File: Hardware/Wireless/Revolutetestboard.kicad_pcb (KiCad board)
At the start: 4 copper layers, 54 x 85.6 mm, 263 parts, among them J1 Conn_01x02_Pin, J2 Conn_01x02_Pin, J3 Conn_01x02_Pin, J4 Conn_01x04_Socket, J5 Conn_01x02_Pin, J6 Conn_01x04_Pin, J7 USB_C_Receptacle_USB2.0, J8 USB_C_Receptacle_USB2.0, J9 Conn_01x04_Socket, Q1 NMOS-CSD17381F4, Q10 PMOS-BSS84, Q2 NMOS-CSD17381F4, Q3 PMOS-CSD25483F4, Q4 PMOS-CSD25483F4, Q5 PMOS-CSD25483F4, Q7 PMOS-BSS84, Q8 IRLML6344, Q9 PMOS-BSS84, SW1 SW_DIP_x06, SW2 SW_DPDT_x2, SW3 SW_DIP_x06, SW4 SW_Push, SW5 SW_DPDT_x2, SW6 SW_DPDT_x2, U1 BQ27427, U10 battery_charger, U11 nRF52840_aQFN73, U12 TS5A3159AYZPR, U13 BQ27427, U14 TPS22910A, U15 A3144e, U16 A3144e, U18 pogopins, U19 LSM6DS3, U2 nrf52833_qfn40, U20 TPS54202DDC, U21 TPS54202DDC, U22 STM32F103CBTx, U23 AP2112K-3.3, U24 Conn_01x14_Socket, U25 TLV493D, U3 Conn_01x14_Socket, U4 TPS709, U5 AS5600, U6 BQ25180, U7 LSM6DSO, U8 TS5A3159AYZPR, U9 TPS22910A, X1 32.768 kHz, X2 32MHZ, X3 32.768 kHz, X4 32MHZ, Y1 32.768KHZ, Y2 8Mhz

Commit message: test board done
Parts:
- removed D3: RED_LED, LED_SMD:LED_0402_1005Metric
- removed R29: 1K, Resistor_SMD:R_0402_1005Metric
- added R58: 220r, Resistor_SMD:R_0402_1005Metric, F.Cu at (131.1, 130.5)
- added R59: 220r, Resistor_SMD:R_0402_1005Metric, F.Cu at (130.1, 130.7)
- added R7: 220r, Resistor_SMD:R_0402_1005Metric, F.Cu at (132.7, 130.2)
- added U26: 1615 RGB SMD LED, Library:1615 RGB SMD LED, F.Cu at (131.3, 128.2)
- moved JP7 0.23 mm to (132.4, 133.2)
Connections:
- U11 pad B13: /pod/P0.03 -> B-
- U11 pad B15: Net-(D3-A) -> G-
- U11 pad B19: unconnected-(U11-P1.11-PadB19) -> R-
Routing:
- net R-: track 0.00 -> 8.92 mm, vias 0 -> 2
- net Net-(D3-A): track 7.42 -> 0.00 mm, vias 2 -> 0
- net G-: track 0.00 -> 6.68 mm, vias 0 -> 2
- net B-: track 0.00 -> 5.74 mm, vias 0 -> 2
- net Net-(U26-R-): track 0.00 -> 3.02 mm
- net Net-(U26-B-): track 0.00 -> 1.55 mm
- net Net-(U26-G-): track 0.00 -> 1.35 mm
- net Net-(D3-K): track 1.00 -> 0.00 mm
- net /pod/3V: track 11.8 -> 12.7 mm, vias 9 -> 10
- net /pod/COM: track 67.2 -> 67.8 mm

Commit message: finished routing
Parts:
- added TP12: TestPoint, TestPoint:TestPoint_Pad_D1.0mm, B.Cu at (158.8, 139.8)
- added TP13: TestPoint, TestPoint:TestPoint_Pad_D1.0mm, B.Cu at (160.5, 124.8)
- added TP14: TestPoint, TestPoint:TestPoint_Pad_D1.0mm, B.Cu at (156.8, 130.0)
- added TP15: TestPoint, TestPoint:TestPoint_Pad_D1.0mm, B.Cu at (156.8, 128.0)
- added TP18: TestPoint, TestPoint:TestPoint_Pad_D1.0mm, B.Cu at (162.1, 119.5)
- added TP4: TestPoint, TestPoint:TestPoint_Pad_D1.0mm, B.Cu at (148.3, 125.4)
- R14, R32: value 50r -> *50r
- moved TP1 5.28 mm to (150.9, 125.2)
- moved C25 4.69 mm to (150.1, 137.4), turned to 180 degrees
- moved R14 3.92 mm to (151.8, 135.4), turned to -90 degrees
- moved C22 2.54 mm to (153.7, 137.3), turned to 0 degrees
- moved R33 0.10 mm to (121.1, 137.4)
- turned U8 to -90 degrees
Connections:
- R14 pad 2: /rev/COM -> /rev/TX_TS5A3159AYZPR
- R32 pad 2: /pod/COM -> /pod/RX_TS5A3159AYZPR
- R8 pad 1: /rev/P0.17 -> /rev/P0.15
- R9 pad 1: /rev/P0.15 -> /rev/P0.17
- U12 pad A1: /pod/RX_TS5A3159AYZPR -> /pod/COM
- U12 pad C2: /pod/COM -> /pod/RX_TS5A3159AYZPR
- U6 pad B1: /rev/P0.17 -> /rev/P0.15
- U6 pad C1: /rev/P0.15 -> /rev/P0.17
- U8 pad A1: /rev/TX_TS5A3159AYZPR -> /rev/COM
- U8 pad C2: /rev/COM -> /rev/TX_TS5A3159AYZPR
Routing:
- net /rev/vSYSTEM: track 0.00 -> 11.7 mm
- net /rev/P0.15: track 55.1 -> 48.1 mm, vias 6 -> 5
- net /rev/COM: track 0.00 -> 5.47 mm, vias 0 -> 1
- net /rev/MOS_VDD: track 6.30 -> 2.72 mm
- net /pod/SDA: track 59.9 -> 57.1 mm
- net /rev/IN_TS5A3159AYZPR: track 18.8 -> 21.5 mm
- net /rev/P0.09: track 29.4 -> 26.9 mm
- net /rev/P0.31: track 24.4 -> 26.8 mm
- net /rev/Batteryin: track 26.0 -> 28.2 mm
- net /rev/P0.17: track 48.6 -> 46.4 mm, vias 4 -> 6
- net /rev/INT: track 13.0 -> 10.7 mm
- net /rev/ON_TPS22910A: track 20.1 -> 22.3 mm
- net /rev/int1: track 13.2 -> 15.4 mm
- net /rev/VDD_nRF: track 11.1 -> 9.03 mm
- net Net-(BT1-+): track 11.7 -> 12.9 mm
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- added copper zone on F.Cu, net /pod/MOS_LED_5V
- added copper zone on F.Cu, net /pod/SDA
- added copper zone on F.Cu, net /rev/INT
- added copper zone on F.Cu, net /rev/P0.15
- added copper zone on F.Cu, net /rev/P0.17
- added copper zone on F.Cu, net /rev/VBUS
- added copper zone on F.Cu, net /rev/vBAT
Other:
- board text added: "+"
- board text added: "-"
- board text added: "1.8V"
- board text added: "5V"
- board text added: "BAT BRIDGE"
- board text added: "BAT CONN"
- board text added: "BAT OFF BRIDGE"
- board text added: "BAT_P"
- board text added: "Bat in"
- board text added: "COM"
- board text added: "G"
- board text added: "GND"
- board text added: "MOS"
- board text added: "MOS_VDD"
- board text added: "P0.31"
- board text added: "PCB THICKNESS: 1mm"
- board text added: "POD1"
- board text added: "POD2"
- board text added: "POD⇵BRIDGE"
- board text added: "REV"
- board text added: "RX"
- board text added: "Revolute Dev Kit"
- board text added: "STACKUP: JLC04101H-7628"
- board text added: "TX"
- board text added: "VBUS"
- board text added: "VDD"
- board text added: "VSYS"
- board text added: "vBAT"

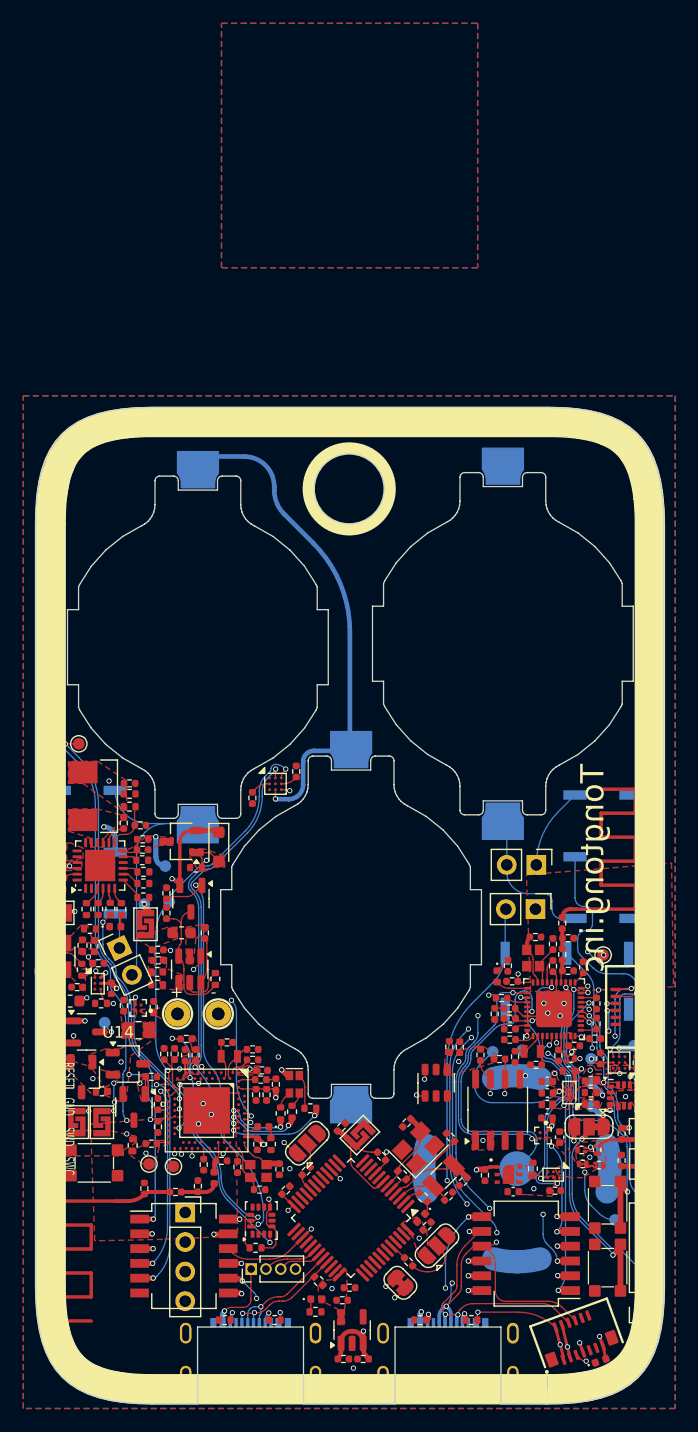
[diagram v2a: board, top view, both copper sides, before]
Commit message: centered flex pcb, made pcb 1.6mm
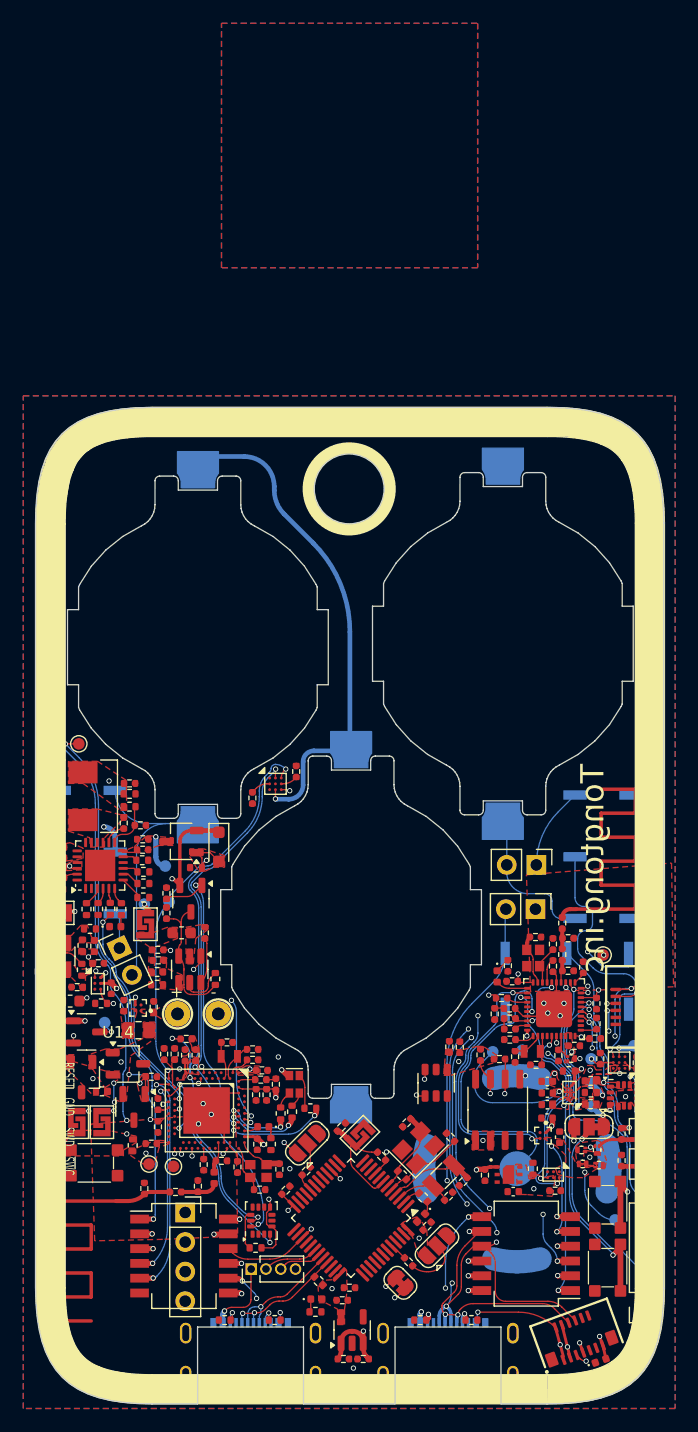
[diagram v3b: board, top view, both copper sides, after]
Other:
- board text added: "PCB THICKNESS: 1.6mm"
- board text added: "STACKUP: JLC04161H-7628"
- board text removed: "PCB THICKNESS: 1mm"
- board text removed: "STACKUP: JLC04101H-7628"
